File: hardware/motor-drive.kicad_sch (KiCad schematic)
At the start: 3 parts, among them J1 USB_C_Receptacle_USB2.0_14P

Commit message: Define footprints
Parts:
- J1: footprint (none) -> Connector_USB:USB_C_Receptacle_Palconn_UTC16-G
- R3, R4: footprint (none) -> Resistor_SMD:R_0402_1005Metric
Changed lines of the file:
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@@
 			)
 		)
-		(property "Footprint" ""
+		(property "Footprint" "Resistor_SMD:R_0402_1005Metric"
 			(at 85.852 90.17 90)
 			(effects
@@
 			)
 		)
-		(property "Footprint" ""
+		(property "Footprint" "Resistor_SMD:R_0402_1005Metric"
 			(at 76.962 90.17 90)
 			(effects
@@
 			)
 		)
-		(property "Footprint" ""
+		(property "Footprint" "Connector_USB:USB_C_Receptacle_Palconn_UTC16-G"
 			(at 53.34 93.98 0)
 			(effects

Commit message: MCU layout
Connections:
- net VBUS: no longer names the net of J1.A4 (VBUS), J1.A9 (VBUS), J1.B4 (VBUS), J1.B9 (VBUS)
- no-connect marks 0 -> 1
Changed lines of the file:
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@@
 	(generator_version "9.0")
 	(paper "A4")
+	(no_connect
+		(at 64.77 78.74)
+	)
 	(wire
 		(pts
@@
 	(wire
 		(pts
-			(xy 68.58 77.47) (xy 68.58 78.74)
-		)
-		(stroke
-			(width 0)
-			(type default)
-		)
-	)
-	(wire
-		(pts
 			(xy 64.77 96.52) (xy 64.77 99.06)
 		)
@@
 		(pts
 			(xy 64.77 91.44) (xy 64.77 93.98)
-		)
-		(stroke
-			(width 0)
-			(type default)
-		)
-	)
-	(wire
-		(pts
-			(xy 68.58 78.74) (xy 64.77 78.74)
 		)
 		(stroke
@@
 		)
 	)
-	(symbol
-		(lib_id "power:VBUS")
-		(at 68.58 77.47 0)
-		(unit 1)
-		(exclude_from_sim no)
-		(in_bom yes)
-		(on_board yes)
-		(dnp no)
-		(fields_autoplaced yes)
-		(property "Reference" "#PWR012"
-			(at 68.58 81.28 0)
-			(effects
-				(font
-					(size 1.27 1.27)
-				)
-				(hide yes)
-			)
-		)
-		(property "Value" "VBUS"
-			(at 68.58 72.39 0)
-			(effects
-				(font
-					(size 1.27 1.27)
-				)
-			)
-		)
-		(property "Footprint" ""
-			(at 68.58 77.47 0)
-			(effects
-				(font
-					(size 1.27 1.27)
-				)
-				(hide yes)
-			)
-		)
-		(property "Datasheet" ""
-			(at 68.58 77.47 0)
-			(effects
-				(font
-					(size 1.27 1.27)
-				)
-				(hide yes)
-			)
-		)
-		(property "Description" "Power symbol creates a global label with name \"VBUS\""
-			(at 68.58 77.47 0)
-			(effects
-				(font
-					(size 1.27 1.27)
-				)
-				(hide yes)
-			)
-		)
-		(pin "1"
-		)
-		(instances
-			(project ""
-				(path "/a12b77e7-bd0f-4a70-9ba2-19a87ce48819"
-					(reference "#PWR012")
-					(unit 1)
-				)
-			)
-		)
-	)

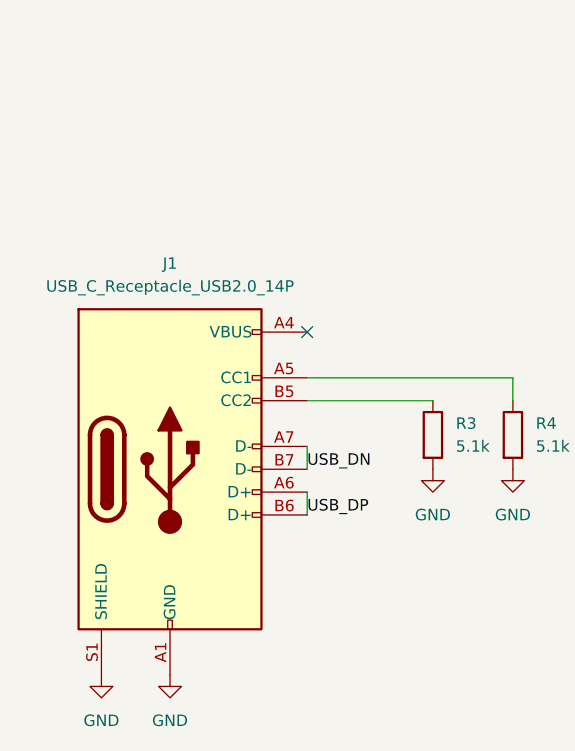
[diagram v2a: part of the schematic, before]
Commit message: Added power connector
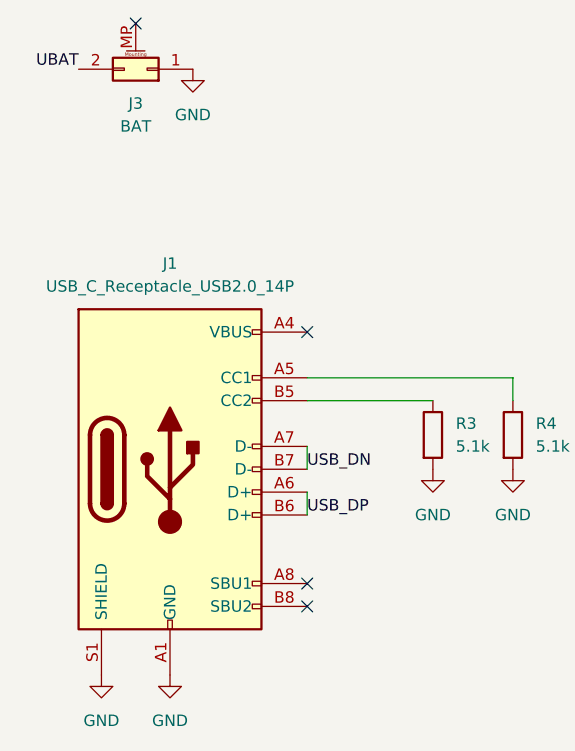
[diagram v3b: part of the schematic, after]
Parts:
- added J3: BAT, Connector_AMASS:AMASS_XT90PW-M_1x02_P10.90mm_Horizontal, symbol Connector_Generic_MountingPin:Conn_02x01_MountingPin
- J1: symbol Connector:USB_C_Receptacle_USB2.0_14P -> Connector:USB_C_Receptacle_USB2.0_16P
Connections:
- net GND: now also J3.1 (Pin_1)
- new net UBAT: J3.2 (Pin_2)
- no-connect marks 1 -> 4
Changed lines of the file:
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@@
 	(paper "A4")
+	(no_connect
+		(at 64.77 109.22)
+	)
+	(no_connect
+		(at 45.72 44.45)
+	)
+	(no_connect
+		(at 64.77 106.68)
+	)
 	(no_connect
 		(at 64.77 78.74)
@@
 	(label "USB_DP"
 		(at 194.31 78.74 180)
+		(effects
+			(font
+				(size 1.27 1.27)
+			)
+			(justify right bottom)
+		)
+	)
+	(label "UBAT"
+		(at 39.37 49.53 180)
 		(effects
 			(font
@@
 	)
 	(symbol
-		(lib_id "Connector:USB_C_Receptacle_USB2.0_14P")
+		(lib_id "Connector:USB_C_Receptacle_USB2.0_16P")
 		(at 49.53 93.98 0)
 		(unit 1)
@@
 			)
 		)
-		(property "Description" "USB 2.0-only 14P Type-C Receptacle connector"
+		(property "Description" "USB 2.0-only 16P Type-C Receptacle connector"
 			(at 49.53 93.98 0)
 			(effects
@@
 		)
 		(pin "A5"
+		)
+		(pin "B8"
+		)
+		(pin "A8"
 		)
 		(instances
@@
 					(unit 1)
 				)
+			)
+		)
+	)
+	(symbol
+		(lib_id "Connector_Generic_MountingPin:Conn_02x01_MountingPin")
+		(at 46.99 49.53 180)
+		(unit 1)
+		(exclude_from_sim no)
+		(in_bom yes)
+		(on_board yes)
+		(dnp no)
+		(fields_autoplaced yes)
+		(property "Reference" "J3"
+			(at 45.72 53.34 0)
+			(effects
+				(font
+					(size 1.27 1.27)
+				)
+			)
+		)
+		(property "Value" "BAT"
+			(at 45.72 55.88 0)
+			(effects
+				(font
+					(size 1.27 1.27)
+				)
+			)
+		)
+		(property "Footprint" "Connector_AMASS:AMASS_XT90PW-M_1x02_P10.90mm_Horizontal"
+			(at 46.99 49.53 0)
+			(effects
+				(font
+					(size 1.27 1.27)
+				)
+				(hide yes)
+			)
+		)
+		(property "Datasheet" "~"
+			(at 46.99 49.53 0)
+			(effects
+				(font
+					(size 1.27 1.27)
+				)
+				(hide yes)
+			)
+		)
+		(property "Description" "Generic connectable mounting pin connector, double row, 02x01, this symbol is compatible with counter-clockwise, top-bottom and odd-even numbering schemes., script generated (kicad-library-utils/schlib/autogen/connector/)"
+			(at 46.99 49.53 0)
+			(effects
+				(font
+					(size 1.27 1.27)
+				)
+				(hide yes)
+			)
+		)
+		(property "LCSC" "C3040689"
+			(at 46.99 49.53 0)
+			(effects
+				(font
+					(size 1.27 1.27)
+				)
+				(hide yes)
+			)
+		)
+		(pin "1"
+		)
+		(pin "2"
+		)
+		(pin "MP"
+		)
+		(instances
+			(project ""
+				(path "/a12b77e7-bd0f-4a70-9ba2-19a87ce48819"
+					(reference "J3")
+					(unit 1)
+				)
+			)
+		)
+	)
+	(symbol
+		(lib_id "power:GND")
+		(at 52.07 49.53 0)
+		(unit 1)
+		(exclude_from_sim no)
+		(in_bom yes)
+		(on_board yes)
+		(dnp no)
+		(fields_autoplaced yes)
+		(property "Reference" "#PWR010"
+			(at 52.07 55.88 0)
+			(effects
+				(font
+					(size 1.27 1.27)
+				)
+				(hide yes)
+			)
+		)
+		(property "Value" "GND"
+			(at 52.07 54.61 0)
+			(effects
+				(font
+					(size 1.27 1.27)
+				)
+			)
+		)
+		(property "Footprint" ""
+			(at 52.07 49.53 0)
+			(effects
+				(font
+					(size 1.27 1.27)
+				)
+				(hide yes)
+			)
+		)
+		(property "Datasheet" ""
+			(at 52.07 49.53 0)
+			(effects
+				(font
+					(size 1.27 1.27)
+				)
+				(hide yes)
+			)
+		)
+		(property "Description" "Power symbol creates a global label with name \"GND\" , ground"
+			(at 52.07 49.53 0)
+			(effects
+				(font
+					(size 1.27 1.27)
+				)
+				(hide yes)
+			)
+		)
+		(pin "1"
+		)
+		(instances
+			(project ""
+				(path "/a12b77e7-bd0f-4a70-9ba2-19a87ce48819"
+					(reference "#PWR010")
+					(unit 1)
+				)

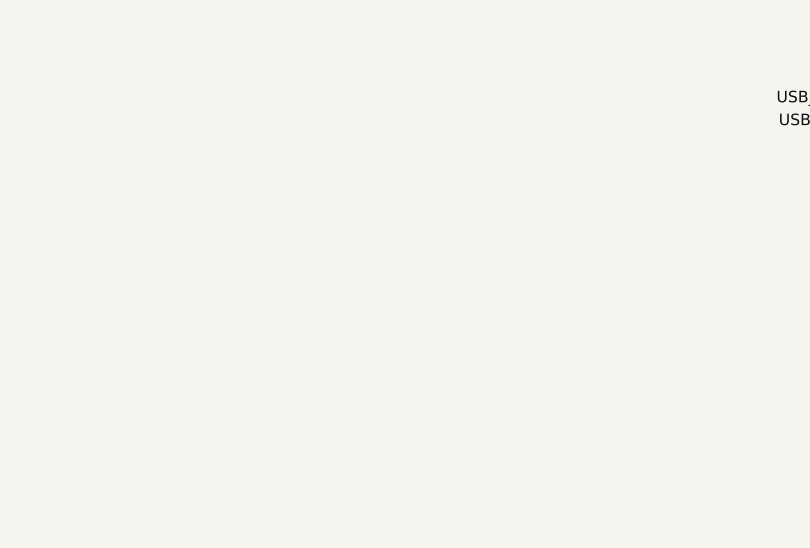
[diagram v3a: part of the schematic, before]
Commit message: Started work on half bridges
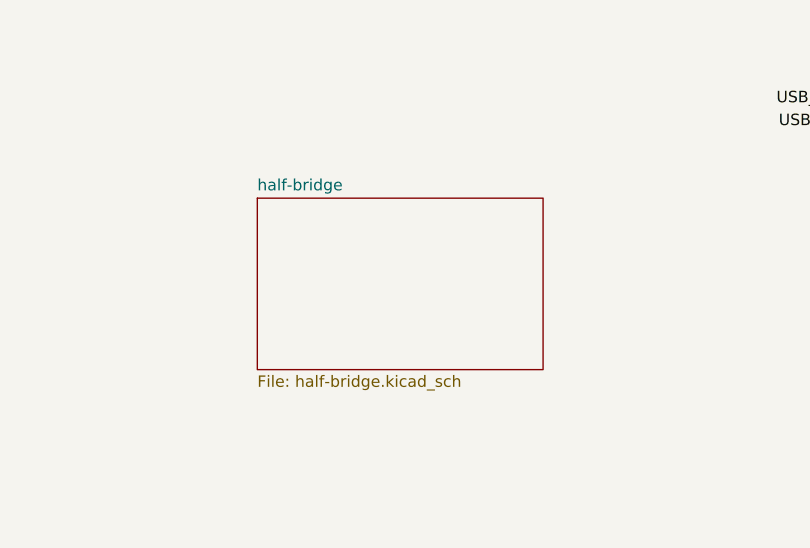
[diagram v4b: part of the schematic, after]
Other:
- added sheet half-bridge (half-bridge.kicad_sch)
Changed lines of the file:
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@@
+		)
+	)
+	(sheet
+		(at 129.54 86.36)
+		(size 31.75 19.05)
+		(exclude_from_sim no)
+		(in_bom yes)
+		(on_board yes)
+		(dnp no)
+		(fields_autoplaced yes)
+		(stroke
+			(width 0.1524)
+			(type solid)
+		)
+		(fill
+			(color 0 0 0 0.0000)
+		)
+		(property "Sheetname" "half-bridge"
+			(at 129.54 85.6484 0)
+			(effects
+				(font
+					(size 1.27 1.27)
+				)
+				(justify left bottom)
+			)
+		)
+		(property "Sheetfile" "half-bridge.kicad_sch"
+			(at 129.54 105.9946 0)
+			(effects
+				(font
+					(size 1.27 1.27)
+				)
+				(justify left top)
+			)
+		)
+		(instances
+			(project "motor-drive"
+				(path "/a12b77e7-bd0f-4a70-9ba2-19a87ce48819"
+					(page "3")
+				)
+			)
 		)
 	)

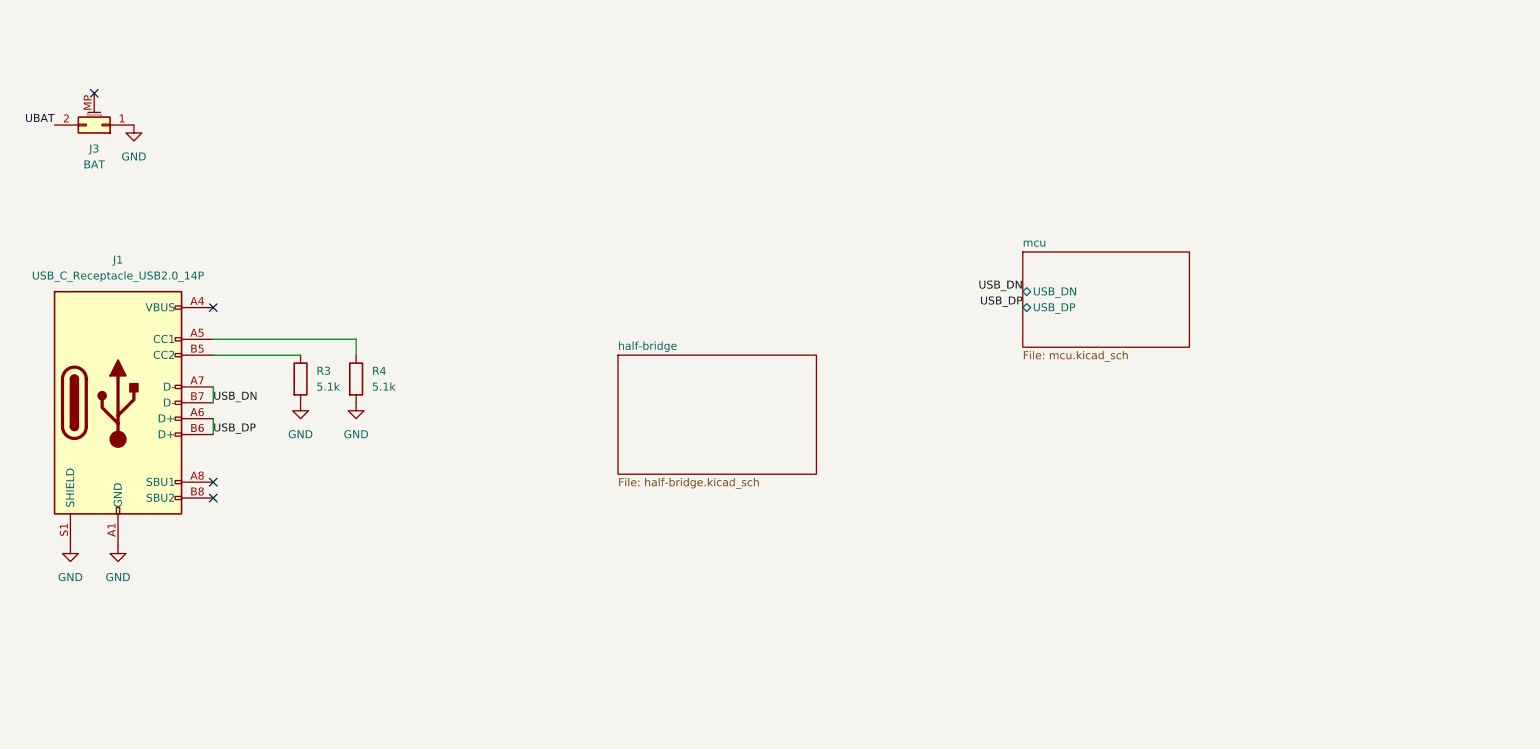
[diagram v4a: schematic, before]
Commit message: Add CAN, USB and sensors
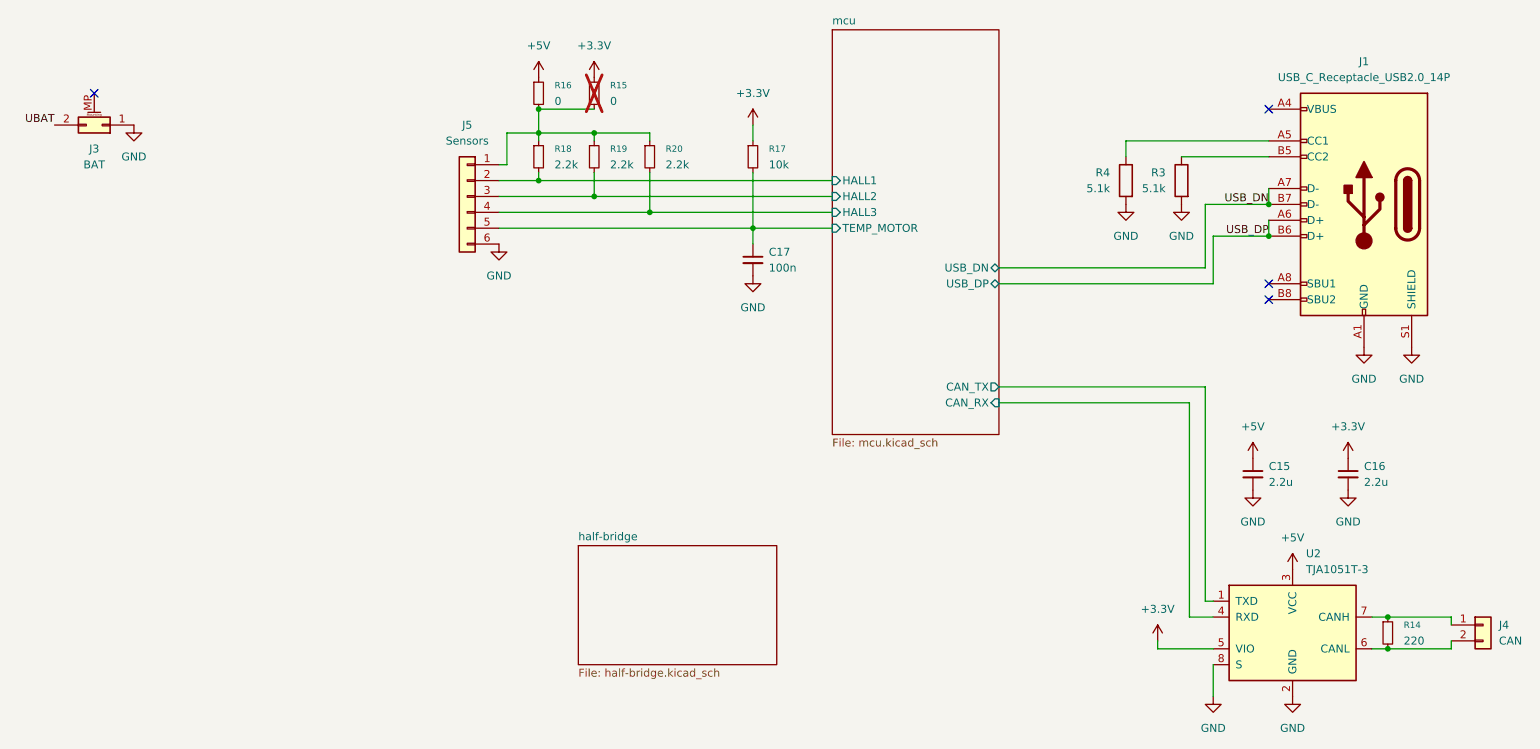
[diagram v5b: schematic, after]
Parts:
- added C15, C16: 2.2u, symbol Device:C_Small
- added C17: 100n, symbol Device:C_Small
- added J4: CAN, symbol Connector_Generic:Conn_01x02
- added J5: Sensors, symbol Connector_Generic:Conn_01x06
- added R14: 220, symbol Device:R_Small
- added R15, R16: 0, symbol Device:R_Small
- added R17: 10k, symbol Device:R_Small
- added R18, R19, R20: 2.2k, symbol Device:R_Small
- added U2: TJA1051T-3, Package_SO:SOIC-8_3.9x4.9mm_P1.27mm, symbol Interface_CAN_LIN:TJA1051T-3
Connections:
- net GND: now also C15.2, C16.2, C17.2, J5.6 (Pin_6), U2.2 (GND), U2.8 (S)
- new net: J5.1 (Pin_1), R15.2, R16.2, R18.1, R19.1, R20.1
- new net: J4.1 (Pin_1), R14.1, U2.7 (CANH)
- new net: J4.2 (Pin_2), R14.2, U2.6 (CANL)
- new net +3.3V: C16.1, R15.1, R17.1, U2.5 (VIO)
- new net +5V: C15.1, R16.1, U2.3 (VCC)
- new net mcu/CAN_RX: U2.4 (RXD)
- new net mcu/CAN_TX: U2.1 (TXD)
- new net mcu/HALL1: J5.2 (Pin_2), R18.2
- new net mcu/HALL2: J5.3 (Pin_3), R19.2
- new net mcu/HALL3: J5.4 (Pin_4), R20.2
- new net mcu/TEMP_MOTOR: C17.1, J5.5 (Pin_5), R17.2
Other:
- sheet mcu ports: added CAN_RX, CAN_TX, HALL1, HALL2, HALL3, TEMP_MOTOR; removed none
- moved on the sheet: J1, R3, R4
